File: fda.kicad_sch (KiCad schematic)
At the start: 43 parts, among them U706 OPA2197D, U73 OPA2388DGK, U74 THS4521IDGK

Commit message: Put in some IO resistors.
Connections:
- net IN+: now also RN72.8; no longer RN72.1
- net IN-: now also RN73.5; no longer RN73.4
- net In+Fb-: now also RN72.1, RN72.2, RN72.3, RN72.4; no longer RN72.5, RN72.6, RN72.7, RN72.8
- net In-Fb+: now also RN73.1, RN73.2, RN73.3, RN73.4; no longer RN73.5, RN73.6, RN73.7, RN73.8
- net Out+: now also RN73.6, RN73.7, RN73.8; no longer RN73.1, RN73.2, RN73.3
- net Out-: now also RN72.5, RN72.6, RN72.7; no longer RN72.2, RN72.3, RN72.4
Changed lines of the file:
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@@
 		)
 		(property "Value" "100p"
-			(at 74.93 149.098 0)
+			(at 73.66 152.146 90)
 			(effects
 				(font
@@
 		)
 		(property "Value" "100p"
-			(at 74.93 61.722 0)
+			(at 73.66 60.706 90)
 			(effects
 				(font
@@
 		(lib_id "Parts:LT5400")
 		(at 77.47 78.74 0)
-		(mirror y)
 		(unit 1)
 		(exclude_from_sim no)
@@
 		)
 		(property "Value" "LT5400-1"
-			(at 82.296 83.82 0)
+			(at 82.55 83.82 0)
 			(effects
 				(font
@@
 		)
 		(property "Footprint" "Parts:MSOP-8-1EP_3x3mm_P0.65mm_EP1.68x1.88mm"
-			(at 70.485 78.74 90)
+			(at 84.455 78.74 90)
 			(effects
 				(font
@@
 		)
 		(property "Datasheet" "0.2ppm/°C matching"
-			(at 75.692 95.504 90)
+			(at 79.248 95.504 90)
 			(effects
 				(font
@@
 		(lib_id "Parts:LT5400")
 		(at 77.47 132.08 0)
-		(mirror y)
 		(unit 1)
 		(exclude_from_sim no)
@@
 		)
 		(property "Footprint" "Parts:MSOP-8-1EP_3x3mm_P0.65mm_EP1.68x1.88mm"
-			(at 70.485 132.08 90)
+			(at 84.455 132.08 90)
 			(effects
 				(font
@@
 		)
 		(property "Datasheet" "0.2ppm/°C matching"
-			(at 68.326 133.604 0)
-			(effects
-				(font
+			(at 86.614 133.604 0)
+			(effects
+				(font

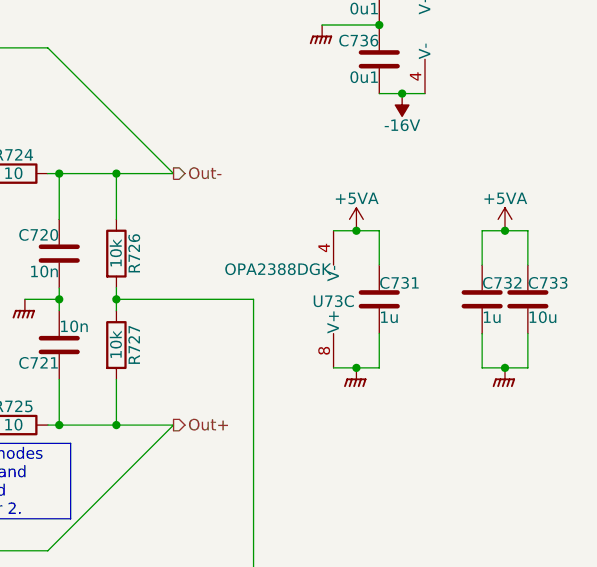
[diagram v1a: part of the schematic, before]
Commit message: DRC update.  Repin ADC.  De-crack the S/H ground.
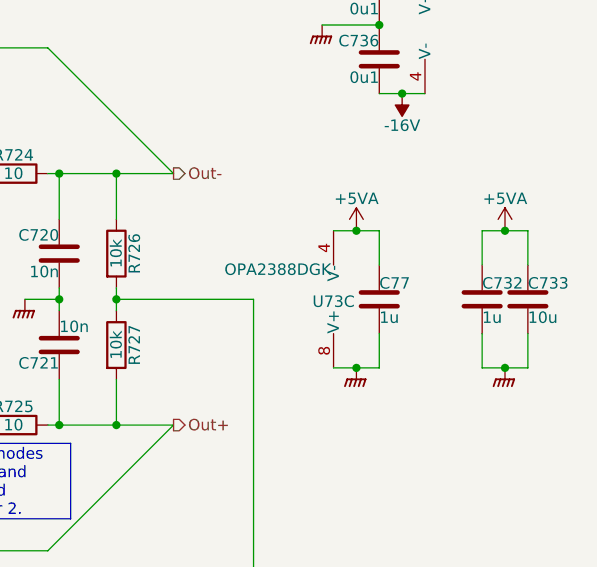
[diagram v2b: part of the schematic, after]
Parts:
- renumbered C731 to C77
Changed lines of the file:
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@@
 		(on_board yes)
 		(dnp no)
-		(property "Reference" "C731"
+		(property "Reference" "C77"
 			(at 179.07 102.362 0)
 			(effects
@@
 			(project "lincal"
 				(path "/b054cef4-39e3-49d8-aff0-7ba5a206c187/91ba7742-b0d4-4498-bde0-79d5f38f349f"
-					(reference "C731")
+					(reference "C77")
 					(unit 1)
 				)

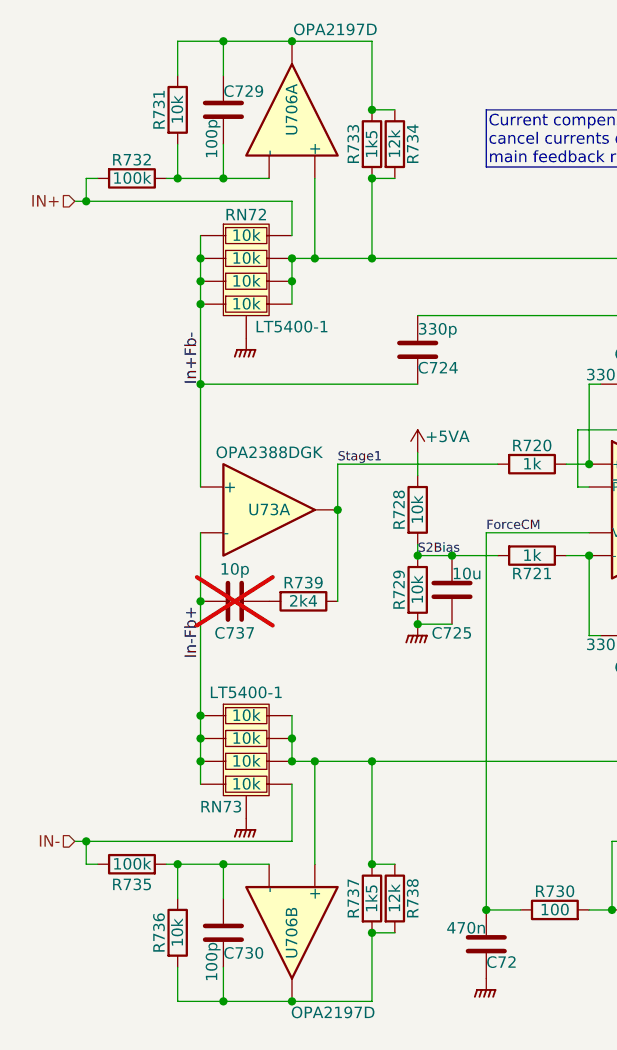
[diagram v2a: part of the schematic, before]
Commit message: More component metadata.
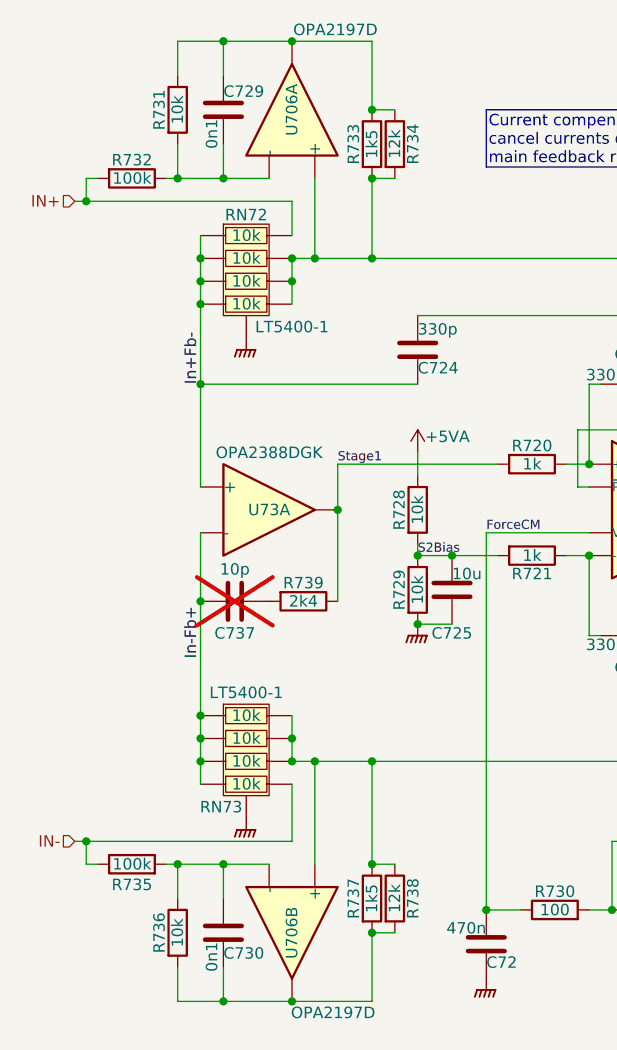
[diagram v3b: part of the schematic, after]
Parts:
- C72, C720, C721, C722, C723, C724, C725, C732, C733, C734, C736, C74, C75, C77, R720, R721, R722, R723, R724, R725, R728, R729, R730, R731, R732, R734, R735, R736, R738, R739, R740, RN72, RN73: Stock (none) -> JLC
- C729, C730: value 100p -> 0n1; LCSC (none) -> C1546; Stock (none) -> JLC
- C737: Stock (none) -> DNP
- R726, R727: Stock (none) -> Digikey
- R733, R737: LCSC (none) -> C22843; Stock (none) -> JLC
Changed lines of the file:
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@@
 			)
 		)
-		(property "Stock" ""
+		(property "Stock" "JLC"
 			(at 128.27 118.11 90)
 			(effects
@@
 			)
 		)
-		(property "Stock" ""
+		(property "Stock" "JLC"
 			(at 83.82 114.3 90)
 			(effects
@@
 			)
 		)
-		(property "Stock" ""
+		(property "Stock" "JLC"
 			(at 128.27 90.17 90)
 			(effects
@@
 			)
 		)
-		(property "Stock" ""
+		(property "Stock" "JLC"
 			(at 120.65 90.17 90)
 			(effects
@@
 			)
 		)
-		(property "Stock" ""
+		(property "Stock" "JLC"
 			(at 109.22 99.06 90)
 			(effects
@@
 			)
 		)
-		(property "Stock" ""
+		(property "Stock" "JLC"
 			(at 69.85 59.69 90)
 			(effects
@@
 			)
 		)
-		(property "Stock" ""
+		(property "Stock" "JLC"
 			(at 138.43 118.11 90)
 			(effects
@@
 			)
 		)
-		(property "Stock" ""
+		(property "Stock" "JLC"
 			(at 143.51 99.06 0)
 			(effects
@@
 			)
 		)
-		(property "Stock" ""
+		(property "Stock" "JLC"
 			(at 179.07 104.14 0)
 			(effects
@@
 			)
 		)
-		(property "Stock" ""
+		(property "Stock" "JLC"
 			(at 96.52 104.14 90)
 			(effects
@@
 			)
 		)
-		(property "Stock" ""
+		(property "Stock" "JLC"
 			(at 134.62 156.21 0)
 			(effects
@@
 			)
 		)
-		(property "LCSC" ""
+		(property "LCSC" "C22843"
 			(at 91.44 147.32 90)
 			(effects
@@
 			)
 		)
-		(property "Stock" ""
+		(property "Stock" "JLC"
 			(at 91.44 147.32 90)
 			(effects
@@
 			)
 		)
-		(property "Stock" ""
+		(property "Stock" "JLC"
 			(at 128.27 82.55 90)
 			(effects
@@
 			)
 		)
-		(property "Stock" ""
+		(property "Stock" "JLC"
 			(at 104.14 152.4 0)
 			(effects
@@
 			)
 		)
-		(property "Stock" ""
+		(property "Stock" "JLC"
 			(at 195.58 104.14 0)
 			(effects
@@
 			)
 		)
-		(property "Stock" ""
+		(property "Stock" "JLC"
 			(at 93.98 147.32 90)
 			(effects
@@
 			)
 		)
-		(property "Stock" ""
+		(property "Stock" "Digikey"
 			(at 149.86 99.06 90)
 			(effects
@@
 			)
 		)
-		(property "Stock" ""
+		(property "Stock" "DNP"
 			(at 76.2 114.3 90)
 			(effects
@@
 			)
 		)
-		(property "Stock" ""
+		(property "Stock" "JLC"
 			(at 96.52 113.03 90)
 			(effects
@@
 			)
 		)
-		(property "LCSC" ""
+		(property "LCSC" "C22843"
 			(at 91.44 63.5 90)
 			(effects
@@
 			)
 		)
-		(property "Stock" ""
+		(property "Stock" "JLC"
 			(at 91.44 63.5 90)
 			(effects
@@
 			)
 		)
-		(property "Stock" ""
+		(property "Stock" "JLC"
 			(at 120.65 118.11 90)
 			(effects
@@
 			)
 		)
-		(property "Stock" ""
+		(property "Stock" "JLC"
 			(at 179.07 69.85 0)
 			(effects
@@
 			)
 		)
-		(property "Stock" ""
+		(property "Stock" "Digikey"
 			(at 149.86 109.22 90)
 			(effects
@@
 			)
 		)
-		(property "Stock" ""
+		(property "Stock" "JLC"
 			(at 69.85 151.13 90)
 			(effects
@@
 			)
 		)
-		(property "Value" "100p"
+		(property "Value" "0n1"
 			(at 73.66 152.146 90)
 			(effects
@@
 			)
 		)
-		(property "LCSC" ""
+		(property "LCSC" "C1546"
 			(at 74.93 151.13 0)
 			(effects
@@
 			)
 		)
-		(property "Stock" ""
+		(property "Stock" "JLC"
 			(at 74.93 151.13 0)
 			(effects
@@
 			)
 		)
-		(property "Stock" ""
+		(property "Stock" "JLC"
 			(at 109.22 109.22 90)
 			(effects
@@
 			)
 		)
-		(property "Stock" ""
+		(property "Stock" "JLC"
 			(at 125.73 140.97 90)
 			(effects
@@
 			)
 		)
-		(property "Stock" ""
+		(property "Stock" "JLC"
 			(at 96.52 86.36 0)
 			(effects
@@
 			)
 		)
-		(property "Value" "100p"
+		(property "Value" "0n1"
 			(at 73.66 60.706 90)
 			(effects
@@
 			)
 		)
-		(property "LCSC" ""
+		(property "LCSC" "C1546"
 			(at 74.93 59.69 0)
 			(effects
@@
 			)
 		)
-		(property "Stock" ""
+		(property "Stock" "JLC"
 			(at 74.93 59.69 0)
 			(effects
@@
 			)
 		)
-		(property "Stock" ""
+		(property "Stock" "JLC"
 			(at 93.98 63.5 90)
 			(effects
@@
 			)
 		)
-		(property "Stock" ""
+		(property "Stock" "JLC"
 			(at 111.76 148.59 90)
 			(effects
@@
 			)
 		)
-		(property "Stock" ""
+		(property "Stock" "JLC"
 			(at 138.43 90.17 90)
 			(effects
@@
 			)
 		)
-		(property "Stock" ""
+		(property "Stock" "JLC"
 			(at 77.47 78.74 0)
 			(effects
@@
 			)
 		)
-		(property "Stock" ""
+		(property "Stock" "JLC"
 			(at 64.77 143.51 90)
 			(effects
@@
 			)
 		)
-		(property "Stock" ""
+		(property "Stock" "JLC"
 			(at 100.33 113.03 0)
 			(effects
@@
 			)
 		)
-		(property "Stock" ""
+		(property "Stock" "JLC"
 			(at 64.77 67.31 90)
 			(effects
@@
 			)
 		)
-		(property "Stock" ""
+		(property "Stock" "JLC"
 			(at 179.07 77.47 0)
 			(effects
@@
 			)
 		)
-		(property "Stock" ""
+		(property "Stock" "JLC"
 			(at 77.47 132.08 0)
 			(effects
@@
 			)
 		)
-		(property "Stock" ""
+		(property "Stock" "JLC"
 			(at 190.5 104.14 0)
 			(effects
@@
 			)
 		)
-		(property "Stock" ""
+		(property "Stock" "JLC"
 			(at 143.51 109.22 0)
 			(effects

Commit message: Front panel
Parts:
- added C726: 10u, Capacitor_SMD:C_0603_1608Metric, symbol Device:C
- R728: value 10k -> 15k; LCSC C25744 -> C25756
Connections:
- net +5VA: now also C726.1
- net GNDPWR: now also C726.2
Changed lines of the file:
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@@
 	)
 	(junction
+		(at 195.58 96.52)
+		(diameter 0)
+		(color 0 0 0 0)
+	)
+	(junction
 		(at 176.53 96.52)
 		(diameter 0)
@@
 	)
 	(junction
+		(at 195.58 111.76)
+		(diameter 0)
+		(color 0 0 0 0)
+	)
+	(junction
 		(at 72.39 90.17)
 		(diameter 0)
@@
 	(wire
 		(pts
+			(xy 200.66 100.33) (xy 200.66 96.52)
+		)
+		(stroke
+			(width 0)
+			(type default)
+		)
+	)
+	(wire
+		(pts
 			(xy 190.5 107.95) (xy 190.5 111.76)
 		)
@@
 	(wire
 		(pts
+			(xy 200.66 107.95) (xy 200.66 111.76)
+		)
+		(stroke
+			(width 0)
+			(type default)
+		)
+	)
+	(wire
+		(pts
 			(xy 114.3 95.25) (xy 114.3 101.6)
 		)
@@
 	(wire
 		(pts
+			(xy 195.58 96.52) (xy 200.66 96.52)
+		)
+		(stroke
+			(width 0)
+			(type default)
+		)
+	)
+	(wire
+		(pts
 			(xy 143.51 118.11) (xy 149.86 118.11)
 		)
@@
 	(wire
 		(pts
+			(xy 195.58 111.76) (xy 200.66 111.76)
+		)
+		(stroke
+			(width 0)
+			(type default)
+		)
+	)
+	(wire
+		(pts
 			(xy 74.93 67.31) (xy 80.01 67.31)
 		)
@@
 			)
 		)
-		(property "Value" "10k"
+		(property "Value" "15k"
 			(at 96.52 104.14 90)
 			(effects
@@
 			)
 		)
-		(property "LCSC" "C25744"
+		(property "LCSC" "C25756"
 			(at 96.52 104.14 90)
 			(effects
@@
 					(unit 1)
 				)
+			)
+		)
+	)
+	(symbol
+		(lib_id "Device:C")
+		(at 200.66 104.14 0)
+		(unit 1)
+		(exclude_from_sim no)
+		(in_bom yes)
+		(on_board yes)
+		(dnp no)
+		(property "Reference" "C726"
+			(at 200.66 102.362 0)
+			(effects
+				(font
+					(size 1.27 1.27)
+				)
+				(justify left)
+			)
+		)
+		(property "Value" "10u"
+			(at 200.66 106.172 0)
+			(effects
+				(font
+					(size 1.27 1.27)
+				)
+				(justify left)
+			)
+		)
+		(property "Footprint" "Capacitor_SMD:C_0603_1608Metric"
+			(at 201.6252 107.95 0)
+			(effects
+				(font
+					(size 1.27 1.27)
+				)
+				(hide yes)
+			)
+		)
+		(property "Datasheet" "25V"
+			(at 200.66 104.14 0)
+			(effects
+				(font
+					(size 1.27 1.27)
+				)
+				(hide yes)
+			)
+		)
+		(property "Description" "Unpolarized capacitor"
+			(at 200.66 104.14 0)
+			(effects
+				(font
+					(size 1.27 1.27)
+				)
+				(hide yes)
+			)
+		)
+		(property "LCSC" "C96446"
+			(at 200.66 104.14 0)
+			(effects
+				(font
+					(size 1.27 1.27)
+				)
+				(hide yes)
+			)
+		)
+		(property "Stock" "JLC"
+			(at 200.66 104.14 0)
+			(effects
+				(font
+					(size 1.27 1.27)
+				)
+				(hide yes)
+			)
+		)
+		(pin "1"
+		)
+		(pin "2"
+		)
+		(instances
+			(project "lincal"
+				(path "/b054cef4-39e3-49d8-aff0-7ba5a206c187/91ba7742-b0d4-4498-bde0-79d5f38f349f"
+					(reference "C726")
+					(unit 1)
+				)

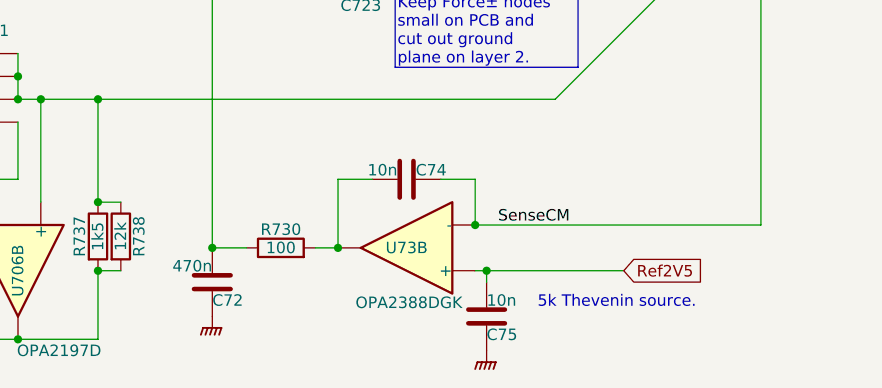
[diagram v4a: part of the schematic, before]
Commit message: Tweak various feedback loops.
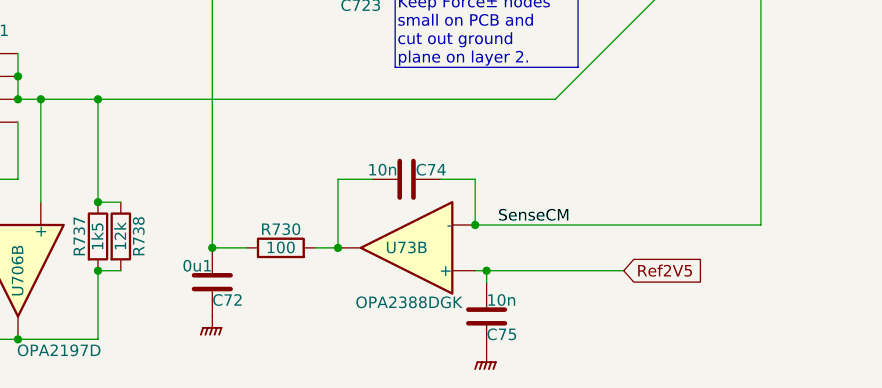
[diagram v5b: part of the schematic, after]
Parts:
- C72: value 470n -> 0u1; LCSC C47339 -> C307331
- U73: Stock 14 -> 14+LCSC
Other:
- note removed: "5k Thevenin source."

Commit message: Readyish
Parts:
- C720, C721, C74, C75: LCSC C307500 -> C389113
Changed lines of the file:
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@@
 			)
 		)
-		(property "Datasheet" "C0G, 25V"
+		(property "Datasheet" "C0G, 50V"
 			(at 143.51 99.06 0)
 			(effects
@@
 			)
 		)
-		(property "LCSC" "C307500"
+		(property "LCSC" "C389113"
 			(at 143.51 99.06 0)
 			(effects
@@
 			)
 		)
-		(property "Datasheet" "C0G, 25V"
+		(property "Datasheet" "C0G, 50V"
 			(at 134.62 156.21 0)
 			(effects
@@
 			)
 		)
-		(property "LCSC" "C307500"
+		(property "LCSC" "C389113"
 			(at 134.62 156.21 0)
 			(effects
@@
 			)
 		)
-		(property "Datasheet" "C0G, 25V"
+		(property "Datasheet" "C0G, 50V"
 			(at 125.73 140.97 0)
 			(effects
@@
 			)
 		)
-		(property "LCSC" "C307500"
+		(property "LCSC" "C389113"
 			(at 125.73 140.97 90)
 			(effects
@@
 			)
 		)
-		(property "Datasheet" "C0G, 25V"
+		(property "Datasheet" "C0G, 50V"
 			(at 143.51 109.22 0)
 			(effects
@@
 			)
 		)
-		(property "LCSC" "C307500"
+		(property "LCSC" "C389113"
 			(at 143.51 109.22 0)
 			(effects

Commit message: Add solder practice.  Final touchups.
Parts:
- RN72, RN73: LCSC C1358072 -> C1731035
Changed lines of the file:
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@@
 			)
 		)
-		(property "LCSC" "C1358072"
+		(property "LCSC" "C1731035"
 			(at 77.47 78.74 90)
 			(effects
@@
 			)
 		)
-		(property "LCSC" "C1358072"
+		(property "LCSC" "C1731035"
 			(at 77.47 132.08 90)
 			(effects
